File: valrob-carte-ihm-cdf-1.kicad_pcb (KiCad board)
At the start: 2 copper layers, 55 x 75 mm, 85 parts, among them J1 USB_C_Receptacle_USB2.0_14P, J2 Conn_01x02, J3 Conn_01x02, J4 Conn_01x04_Pin, J5 Conn_01x04_Pin, J6 Conn_01x04_Pin, SW1 SW_Push, SW2 SW_Push, SW3 SW_DIP_x04, SW4 SW_SPDT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

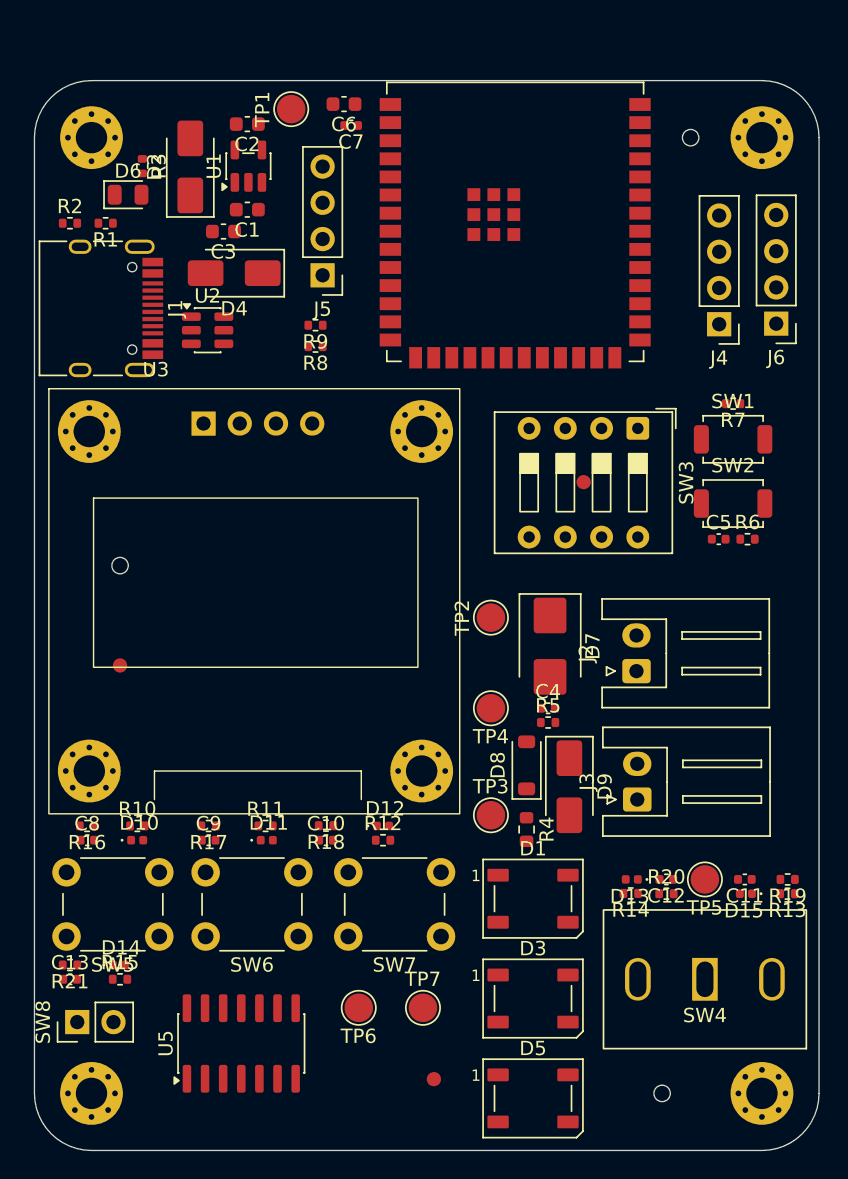
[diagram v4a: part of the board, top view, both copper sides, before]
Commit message: pcb: refine layout
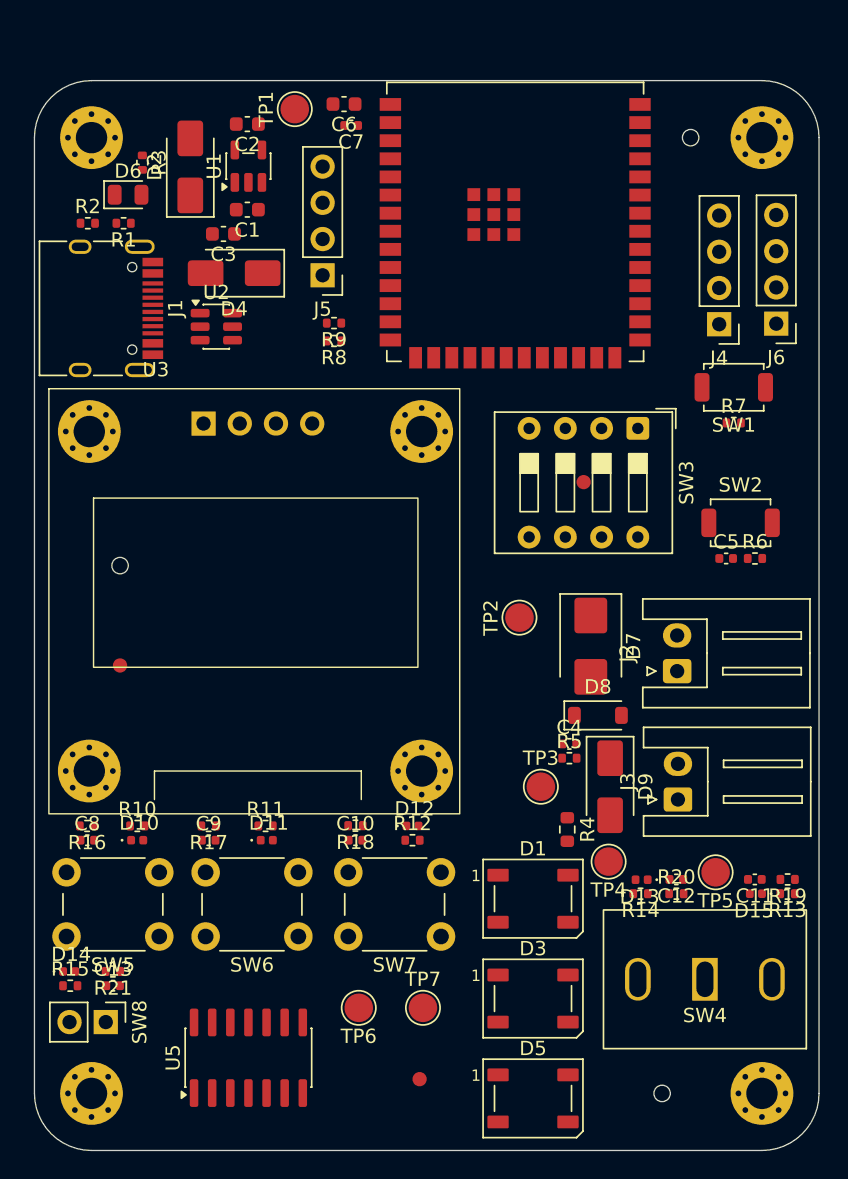
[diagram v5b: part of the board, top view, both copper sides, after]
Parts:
- moved TP4 13.6 mm to (159.2, 122.8)
- moved D8 6.10 mm to (158.5, 112.5), turned to 0 degrees
- moved TP3 4.03 mm to (154.5, 117.5)
- moved SW1 3.65 mm to (168.0, 89.5), turned to 180 degrees
- moved D14 3.52 mm to (121.4, 130.5)
- moved R15 3.52 mm to (121.5, 131.5)
- moved C13 3.04 mm to (124.5, 131.5)
- moved R21 3.04 mm to (124.5, 130.5)
- moved C4 2.91 mm to (156.5, 114.5)
- moved R5 2.91 mm to (156.5, 115.5)
- moved J2 2.85 mm to (164.1, 109.4)
- moved J3 2.85 mm to (164.1, 118.4)
- moved D7 2.85 mm to (158.0, 107.6)
- moved D9 2.85 mm to (159.4, 117.5)
- moved R4 2.85 mm to (156.4, 120.5)
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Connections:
- U5 pad 3: Net-(C12-Pad1) -> Net-(C11-Pad1)
- U5 pad 4: /Switches/ESW2 -> /Switches/ESW3
- U5 pad 5: Net-(C11-Pad1) -> Net-(C12-Pad1)
- U5 pad 6: /Switches/ESW3 -> /Switches/ESW2

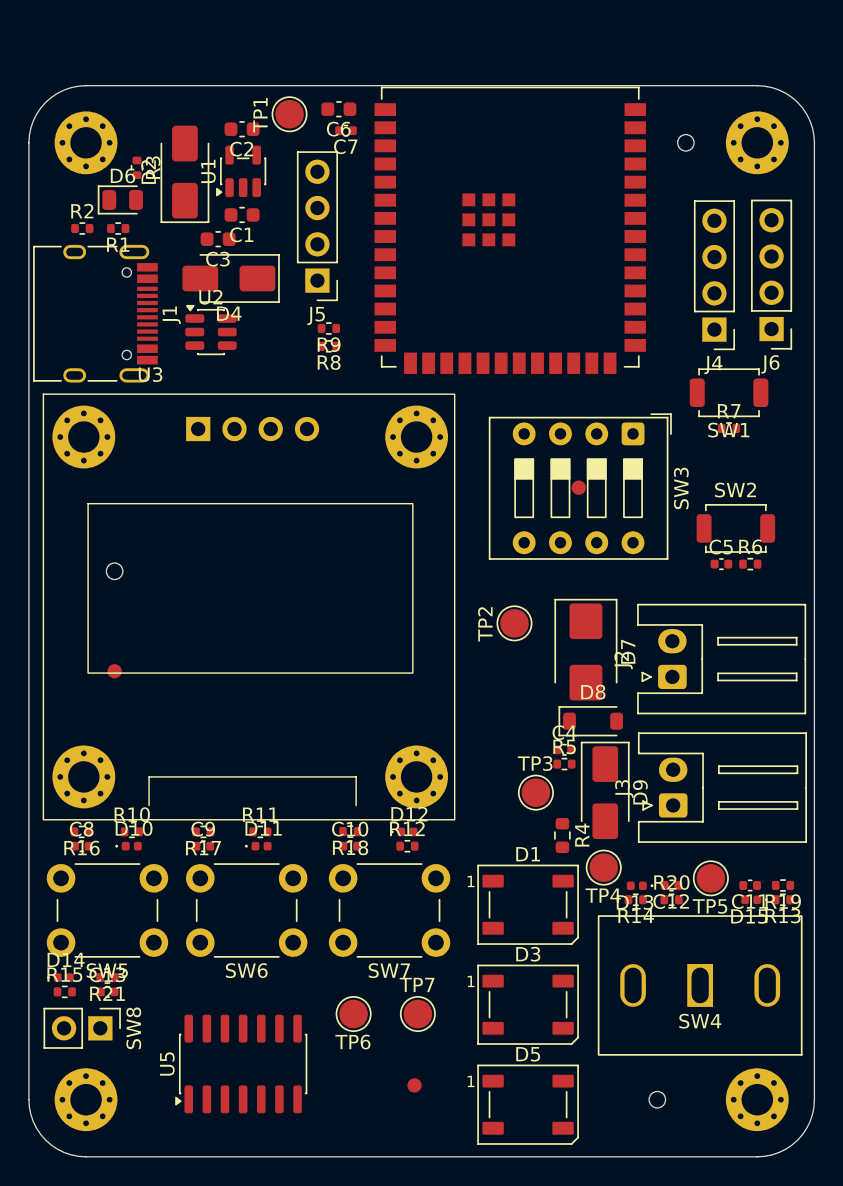
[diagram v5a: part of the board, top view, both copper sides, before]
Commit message: pcb: add ground planes
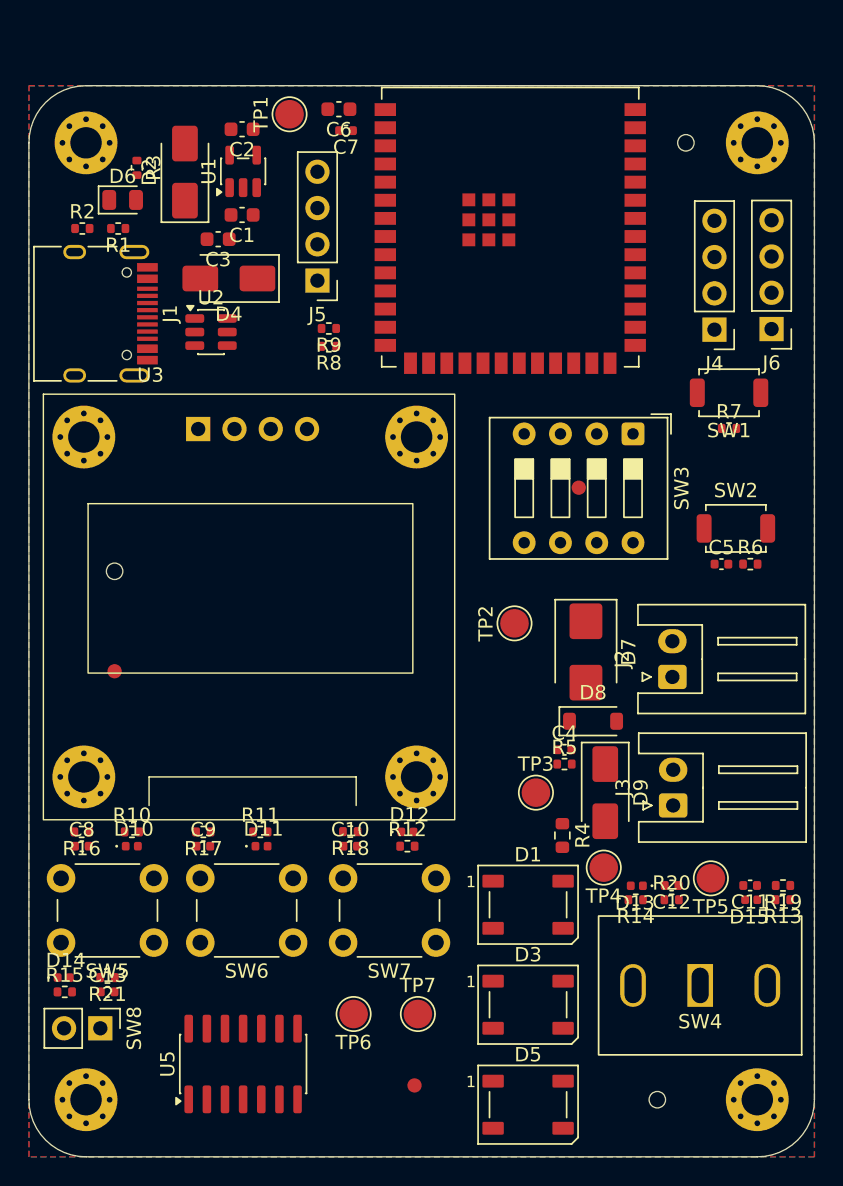
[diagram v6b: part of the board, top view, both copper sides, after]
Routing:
- added copper zone on B.Cu, net GND
- added copper zone on F.Cu, net GND
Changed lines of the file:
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@@
 		(layer "Edge.Cuts")
+	)
+	(zone
+		(net 2)
+		(net_name "GND")
+		(locked yes)
+		(layers "F.Cu" "B.Cu")
+		(hatch edge 0.5)
+		(connect_pads
+			(clearance 0.2)
+		)
+		(min_thickness 0.15)
+		(filled_areas_thickness no)
+		(fill yes
+			(thermal_gap 0.35)
+			(thermal_bridge_width 0.35)
+			(island_removal_mode 1)
+			(island_area_min 10)
+		)
+		(polygon
+			(pts
+				(xy 119 68) (xy 174 68) (xy 174 143) (xy 119 143)
+			)
+		)
 	)
 	(embedded_fonts no)

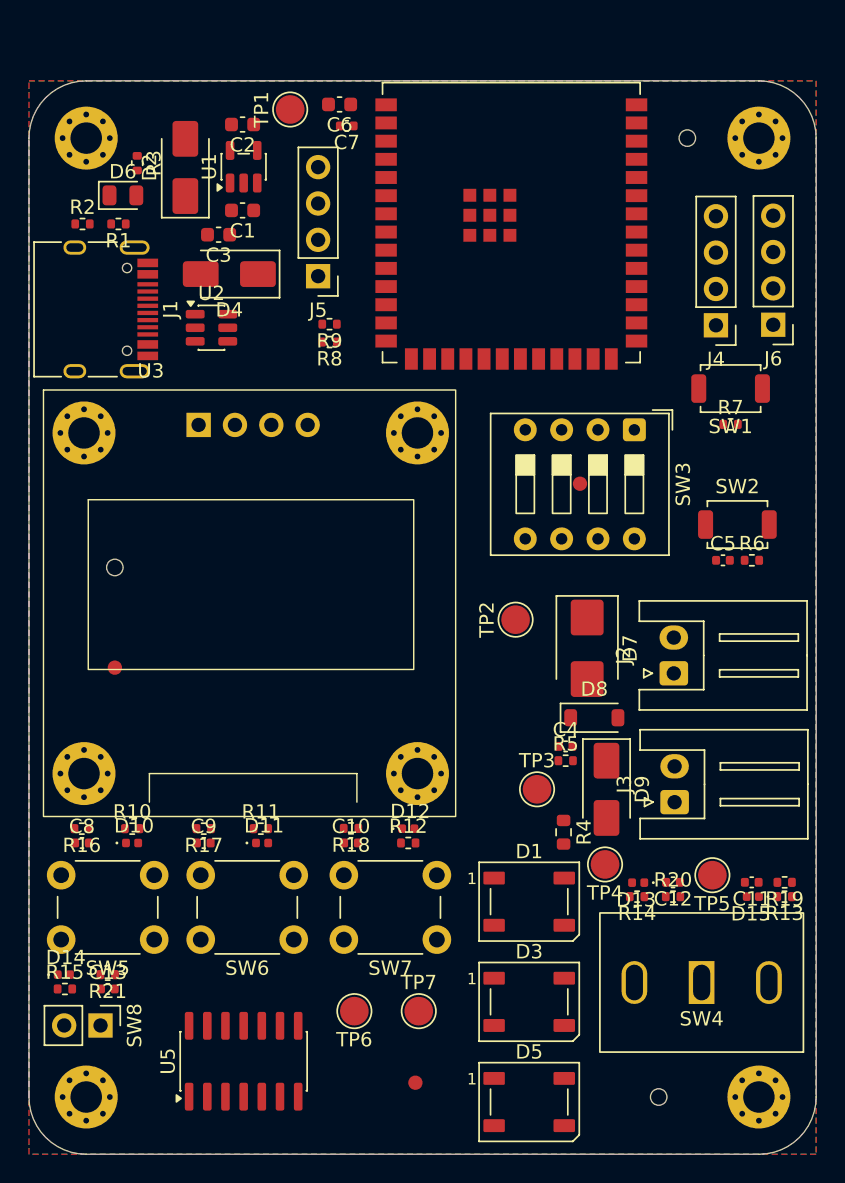
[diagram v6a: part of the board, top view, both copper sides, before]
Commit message: pcb: add gnd vias
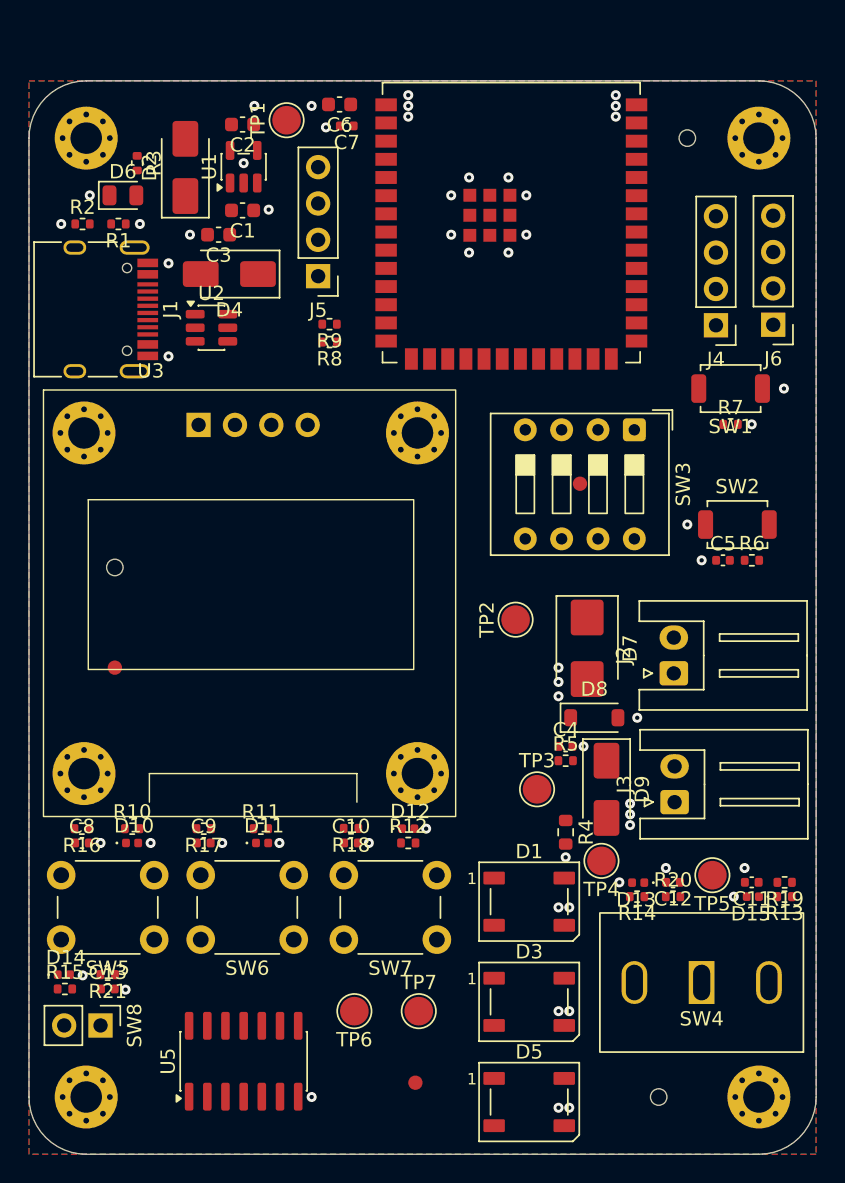
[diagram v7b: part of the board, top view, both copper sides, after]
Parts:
- moved TP1 0.79 mm to (137.0, 70.8)
- moved TP4 0.35 mm to (159.0, 122.5)
- moved R4 0.15 mm to (156.5, 120.5)
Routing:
- net GND: vias 0 -> 57
